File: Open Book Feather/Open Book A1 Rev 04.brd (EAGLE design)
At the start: 77.5 x 112.3 mm, 125 parts, among them J1 SJ-43514-SMT, J2 10118193-0001LF, Q1 DMG341, Q2 IRLML0100, SW1 SPDT_SWITCH, U1 AP2112-3.3, U2 MCP73831T-2ACI/OT, U3 ATSAMD51J64-TQFP(10X10), U4 GD25Q16C (or GD25Q32C), U5 74AC165D, U6 GD25Q16C (or GD25Q32C), U8 MAX4466EXK+T, X1 JSTPH, X2 2x5 0.05" SWD

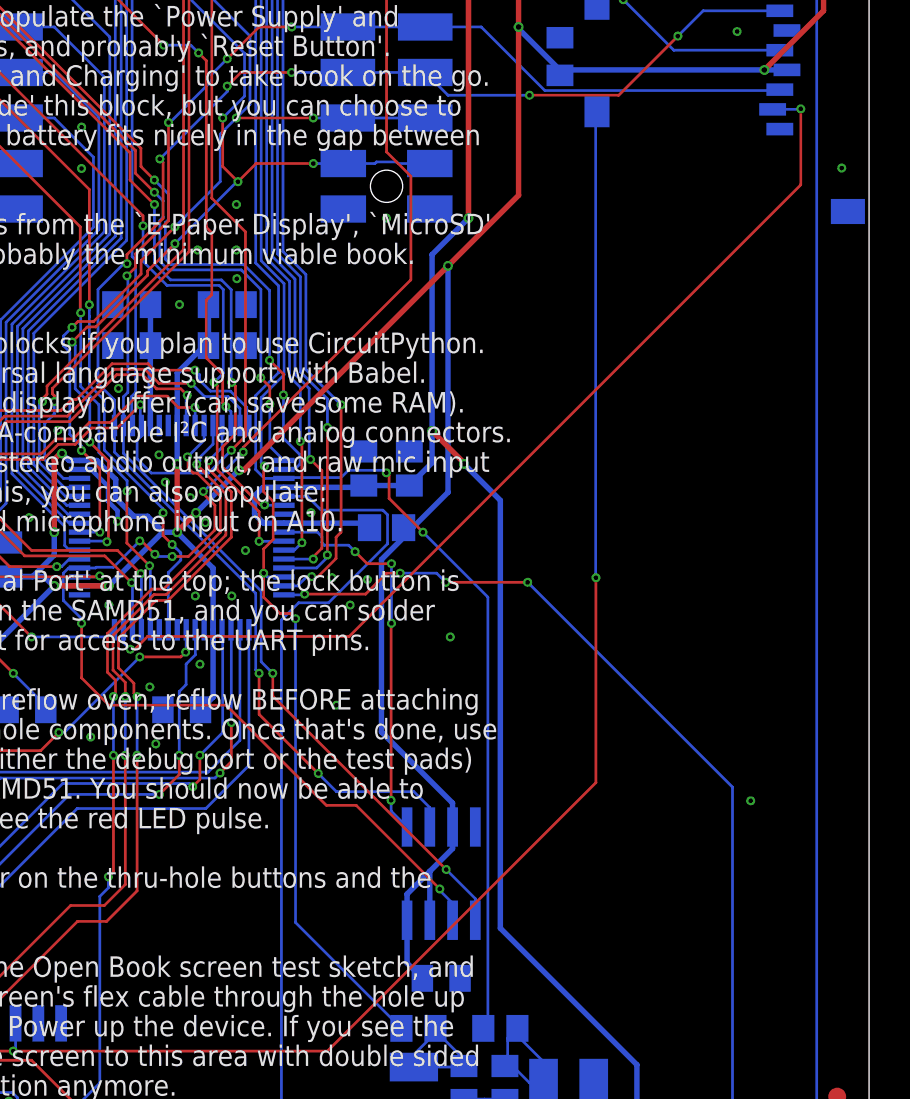
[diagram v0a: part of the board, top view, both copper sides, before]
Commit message: rev 4: move babel chip into SRAM spot
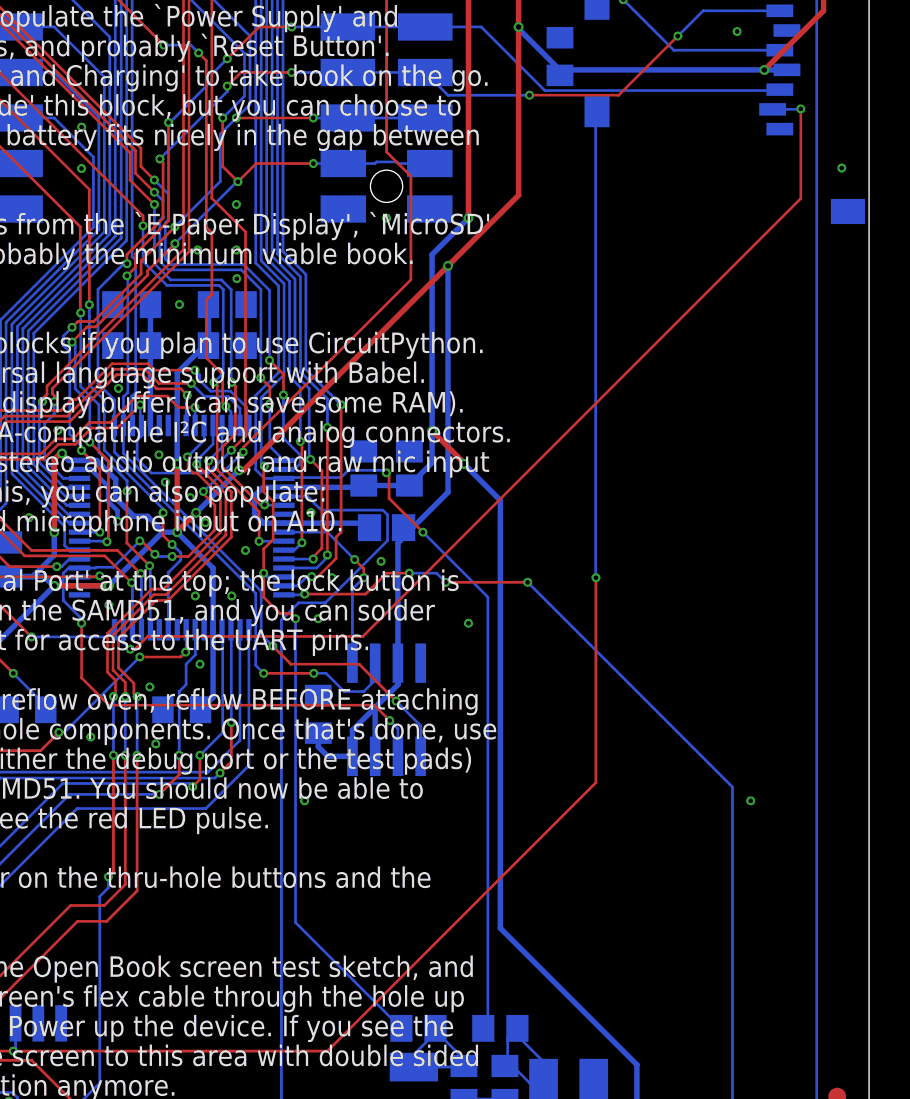
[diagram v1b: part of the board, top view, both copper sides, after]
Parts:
- moved C28 16.3 mm to (46.5, 39.6), turned to 90 degrees
- moved U6 9.64 mm to (50.3, 39.9)
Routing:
- net +3V3: track 518.6 -> 506.7 mm
- net UNIFONT_CS: track 22.0 -> 10.8 mm, vias 4 -> 2
- net MOSI: track 91.7 -> 83.6 mm
- net MISO: track 88.4 -> 81.3 mm
- net SCK: track 105.3 -> 98.8 mm
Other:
- board text added: "U6 is a GD25Q16C Flash chip on the main SPI bus (BCS: D52/PB06). Fits Unicode character data and Unifont glyphs for every codepoint in the Basic Multliingual Plane."
- board text removed: "U6 is a GD25Q16C Flash memory chip on the main SPI bus (BCS: D52/PB06). Stores Unicode character data and Unifont glyphs for every code point in the Basic Multliingual Plane. Contents covered by GPL with font embedding exception."

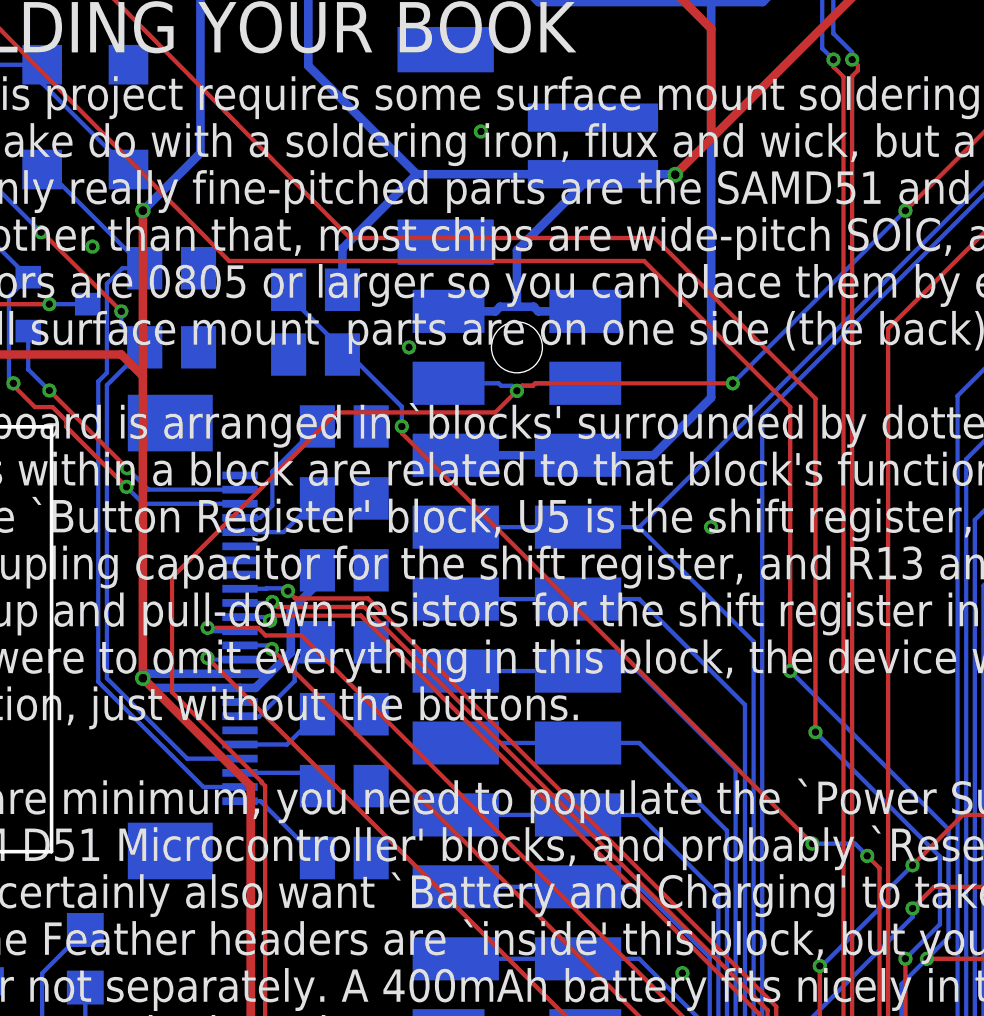
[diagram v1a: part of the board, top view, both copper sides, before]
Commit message: resistor array to monitor both VBAT and VBUS
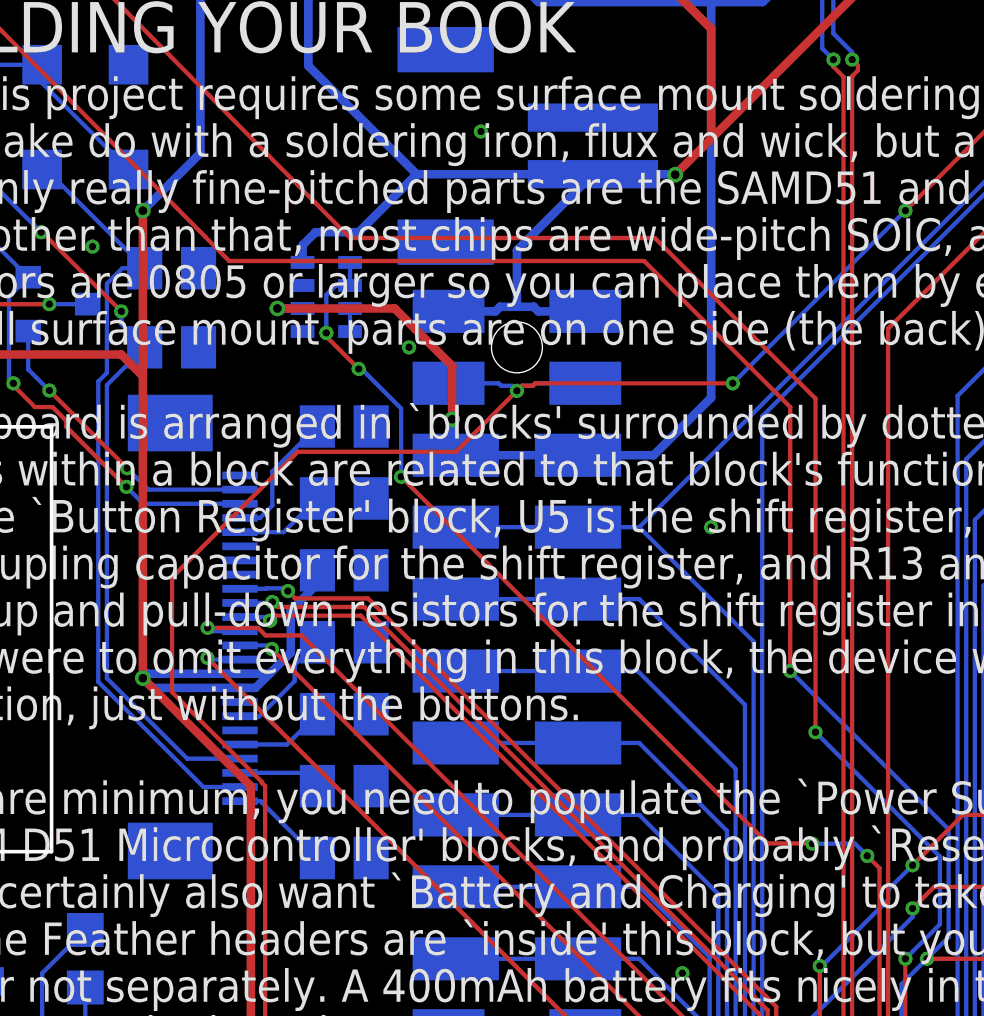
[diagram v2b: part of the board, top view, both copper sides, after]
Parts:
- removed R5: 10K, microbuilder:0805_10MGAP
- R6: value 10K -> 100K; device microbuilder:0805_10MGAP -> resistor array:EXBV8V
- R7: value 100 -> 10K
- R8: value 100K -> 10K; device microbuilder:0805-NO -> microbuilder:0805_10MGAP
- R9: value 100K -> 100; device microbuilder:0805-NO -> microbuilder:0805_10MGAP
- moved R8 90.2 mm to (21.1, 6.35), turned to 270 degrees
- moved R6 89.9 mm to (20.7, 96.3), turned to 0 degrees
- moved R9 87.9 mm to (18.3, 6.35), turned to 90 degrees
- moved R7 35.6 mm to (30.2, 39.9), turned to 180 degrees
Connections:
- removed net A6_VMEAS: R8.2, R9.1, U3.62
- new net A11_BUSMON: R6.3, R6.4
- new net A6_BATMON: R6.1, R6.2, U3.62
- net !RESET: now also R8.2, R9.2; no longer R6.2, R7.2
- net +3V3: now also R7.1, R8.1; no longer R5.1, R6.1
- net GND: now also R6.5, R6.7; no longer R9.2
- net N$1: now also R9.1; no longer R7.1
- net SWCLK: now also R7.2; no longer R5.2
- net VBAT: now also R6.8; no longer R8.1
- net VBUS: now also R6.6
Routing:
- net A6_BATMON: track 0.00 -> 53.2 mm, vias 0 -> 6
- net A6_VMEAS: track 51.3 -> 0.00 mm, vias 4 -> 0
- net VBUS: track 65.4 -> 76.5 mm, vias 2 -> 4
- net A11_BUSMON: track 0.00 -> 0.81 mm
- net VBAT: track 67.9 -> 68.4 mm
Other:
- board text added: "*See notes on this bit at bottom of the POWER SUPPLY block."
- board text added: "An SWD connector (and test points) allow access to the serial wire debug interface. R7=SWCLK pullup"
- board text added: "D1&Q1 conspire to let only the higher of VBAT & VBUS reach 3.3V regulator U1. C1 filters regulator input; C2 & C3 filter output. R1 pulls EN high to keep the regulator on. BATTERY: U2 is a LiPo charging controller. Powered by VBUS, it charges the battery at a rate determined by R3. C4=filter for VBAT, R4 limits current to CHG LED. R6: voltage dividers to gauge VBAT and VBUS on A6/PB01 and (TBD)."
- board text added: "R13-R14 are resistor arrays to keep inputs from floating. C25 (& many small capacitors you see near devices) are bypass caps; they filter current spikes & dips."
- board text added: "R8 pulls !RESET high. Btn pulls it low. C13 is a filter cap. R9 discharges C13. Double tap for UF2 bootloader."
- board text removed: "*Notes on this bit can be found at end of the POWER SUPPLY block."
- board text removed: "An SWD connector (and test points) allow access to the serial wire debug interface. R5=SWCLK pullup"
- board text removed: "D1&Q1 conspire to let only the higher of VBAT & VBUS reach 3.3V regulator U1. C1 filters regulator input; C2 & C3 filter output. R1 pulls EN high to keep the regulator on. BATTERY: U2 is a LiPo charging controller. Powered by VBUS, it charges the battery at a rate determined by R3. C4=filter for VBAT, R4 limits current to CHG LED. R8 & R9 are a voltage divider for VBAT to make a battery gauge on 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"
- board text removed: "R11-R12 are resistor arrays to keep inputs from floating. C25 (& many small capacitors you see near devices) are bypass caps; they filter current spikes & dips."
- board text removed: "R6 pulls !RESET high. Btn pulls it low. C13 is a filter cap. R7 discharges C13. Double tap for UF2 bootloader."

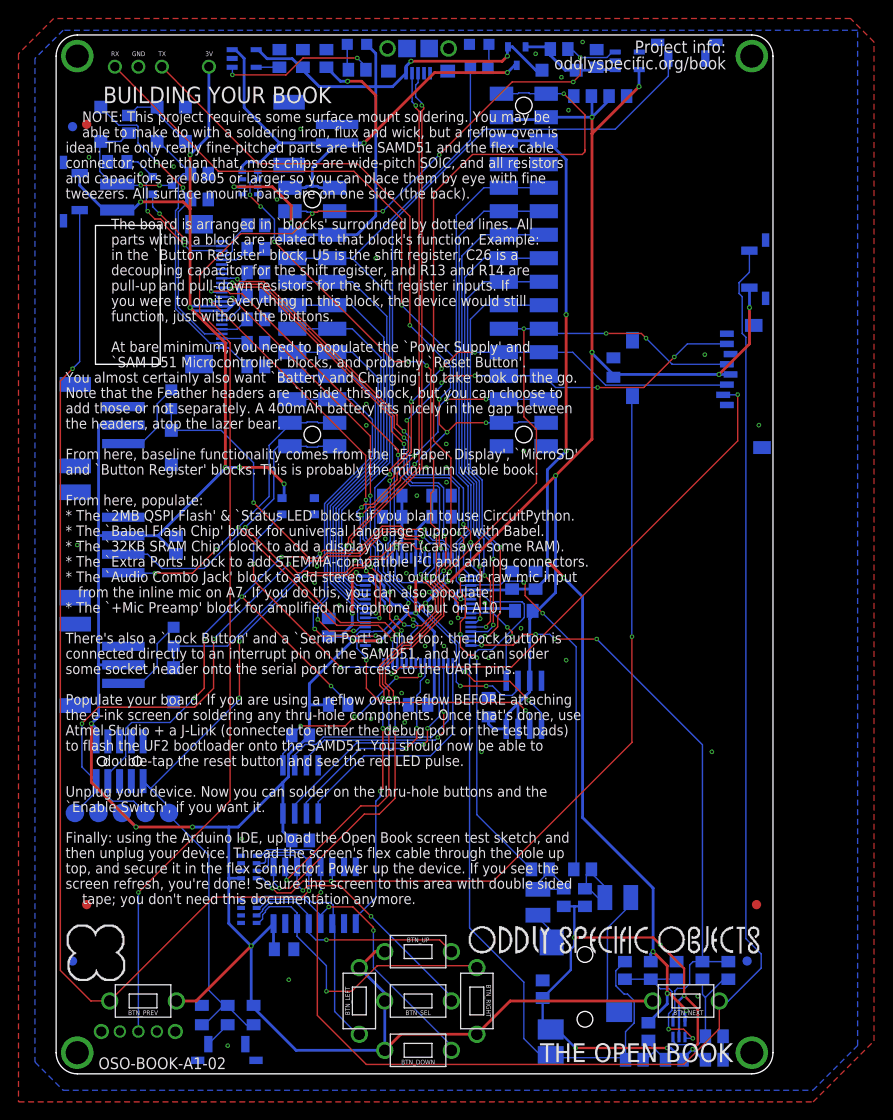
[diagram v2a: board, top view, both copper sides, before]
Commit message: use max4468 for mic amp shutdown capability
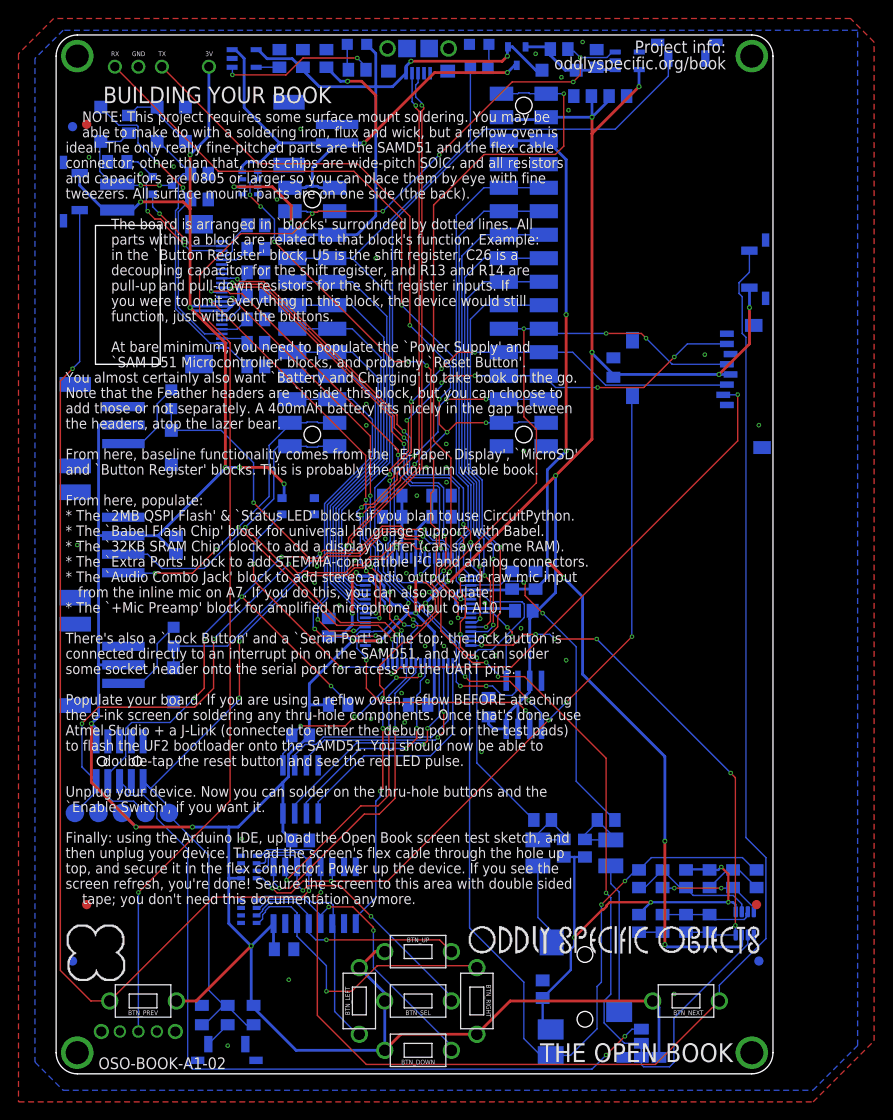
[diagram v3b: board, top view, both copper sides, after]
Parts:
- removed U8: MAX4466EXK+T, microbuilder:SC70-5
- added SJ1: SOLDERJUMPER_FIVEWAY, My Stuff:SOLDERJUMPER_FIVEWAY
- added U7: MAX4468EKAT, MAX4468EKAT:SOT65P280X145-8N
- moved R21 23.6 mm to (75.4, 21.1), turned to 270 degrees
- moved C32 19.9 mm to (70.4, 21.1), turned to 90 degrees
- moved R22 18.9 mm to (72.9, 21.1), turned to 270 degrees
- moved C35 16.8 mm to (62.7, 16.3), turned to 90 degrees
- moved R25 13.4 mm to (65.3, 16.3), turned to 270 degrees
- moved C33 10.0 mm to (62.7, 21.1)
- moved R24 9.99 mm to (65.3, 21.1), turned to 270 degrees
- moved R23 9.96 mm to (67.8, 21.1)
- moved R17 5.91 mm to (59.2, 27.4), turned to 180 degrees
- moved C34 5.47 mm to (70.4, 16.3), turned to 90 degrees
- moved R26 5.38 mm to (67.8, 16.3), turned to 270 degrees
- moved R19 5.34 mm to (52.3, 27.4)
- moved C31 5.33 mm to (51.8, 23.9)
- moved R18 5.33 mm to (56.9, 24.4)
- moved R20 5.33 mm to (54.6, 24.4)
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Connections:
- removed net N$67: C33.2, R23.2, R24.1, U8.1
- new net MICAMP_SHDN: SJ1.2, U7.6
- new net MIC_BIAS_PWR: R22.2, R24.2, U7.4
- new net N$6: C34.2, R25.1, R26.1, U7.3
- new net PB13_SWO_MICSHDN: SJ1.1, U3.60
- new net SWO: SJ1.5, X2.6
- net +3V3: now also SJ1.3
- net A10_MICAMP: now also U7.8; no longer U8.4
- net AGND: now also U7.1; no longer U8.2
- net AVCC: now also U7.7; no longer R22.2, R24.2, U8.5
- net BUTTON_CLK: now also U3.27; no longer U3.60
- net BUTTON_LATCH: now also U3.25; no longer U3.61
- net GND: now also SJ1.4
- net N$68: now also C33.2, R23.2, R24.1, U7.2; no longer C34.2, R25.1, R26.1, U8.3
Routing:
- net SWO: track 0.00 -> 85.8 mm, vias 0 -> 2
- net PB13_SWO_MICSHDN: track 0.00 -> 66.2 mm, vias 0 -> 4
- net MICAMP_SHDN: track 0.00 -> 21.7 mm
- net A7_MIC: track 83.3 -> 101.8 mm, vias 0 -> 2
- net N$67: track 16.6 -> 0.00 mm, vias 2 -> 0
- net BUTTON_CLK: track 46.3 -> 31.4 mm, vias 4 -> 2
- net BUTTON_LATCH: track 49.3 -> 34.6 mm, vias 4 -> 2
- net AGND: track 66.6 -> 52.7 mm, vias 6 -> 4
- net MIC_BIAS_PWR: track 0.00 -> 11.3 mm, vias 0 -> 2
- net N$6: track 0.00 -> 10.0 mm
- net A10_MICAMP: track 65.6 -> 58.0 mm, vias 4 -> 6
- net BUTTON7: track 87.1 -> 80.4 mm, vias 3 -> 5
- net +3V3: track 506.7 -> 513.1 mm
- net AUDIO_LEFT: track 3.56 -> 8.90 mm
- net A1: track 85.0 -> 79.8 mm
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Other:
- board text added: "...on A10/PA07. Turn the amplifier off by setting D48/PB31 high. This also powers down the mic bias circuit R21-C33 to save some power."
- board text added: "Connector and test points give access to SWD interface. R7=SWCLK pullup. See note in mic block about SWO."
- board text added: "DISA"
- board text added: "ENA"
- board text added: "Ferrite bead FB2 isolates AGND from GND."
- board text added: "NOTE: PB31 can do SWO. If you need it (tho you prolly don't): . cut trace btwn PB31 & SHDN, & connect it to SWO. Now tie SHDN to ENA or . DISA to keep the amp on (or off)."
- board text added: "PB31"
- board text added: "Pins: BUTTON_CLOCK: D53/PB14 BUTTON_OUT: D49/PB30 BUTTON_LATCH: D43/PB12"
- board text added: "SHDN"
- board text added: "SWO"
- board text added: "These resistors and capacitors couple analog outputs A0/PA02 and A1/PA05 to R and L channels of the phone jack. A7/PB04 is raw signal from mic input."
- board text added: "U7 is a MAX4468 amp for an inline electret mic (amplified signal..."
- board text removed: "A0/PA02: R audio out A1/PA05: L audio out A7/PB04: Raw mic in"
- board text removed: "Amplified mic signal on A10/PA07"
- board text removed: "An SWD connector (and test points) allow access to the serial wire debug interface. R7=SWCLK pullup"
- board text removed: "Pins: BUTTON_CLOCK: D48/PB31 BUTTON_OUT: D49/PB30 BUTTON_LATCH: D50/PB00"
- board text removed: "U8 is a MAX4466 amp for an inline electret mic."
